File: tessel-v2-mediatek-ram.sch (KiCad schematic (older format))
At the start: 21 parts, among them U201 MT7620N, U301 W9751G6KB-25

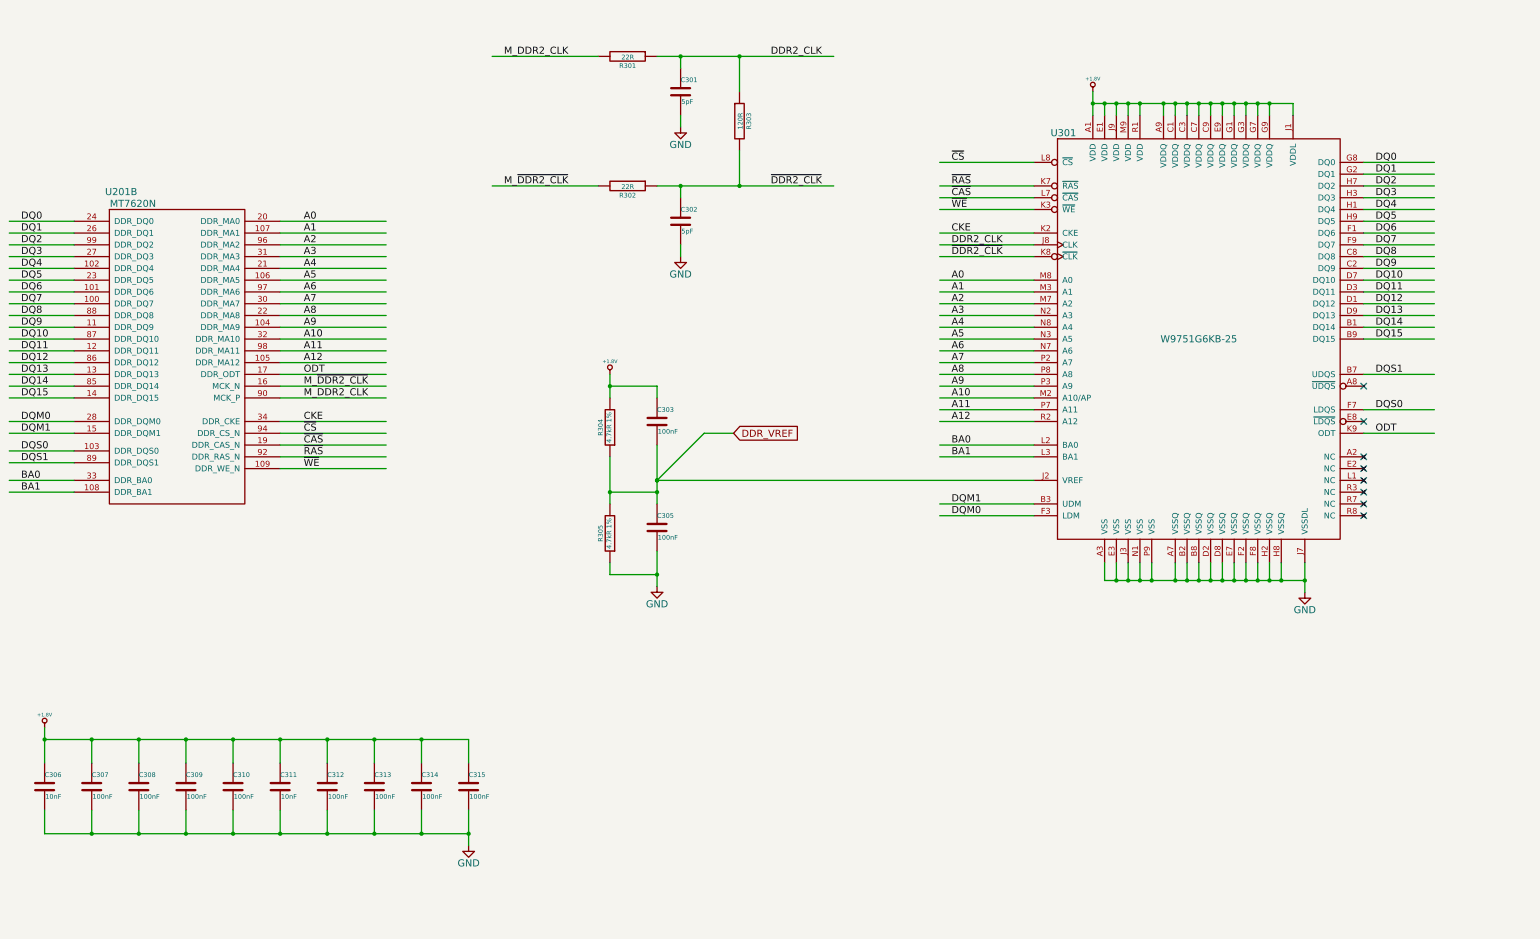
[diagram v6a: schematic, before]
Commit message: reset annotation
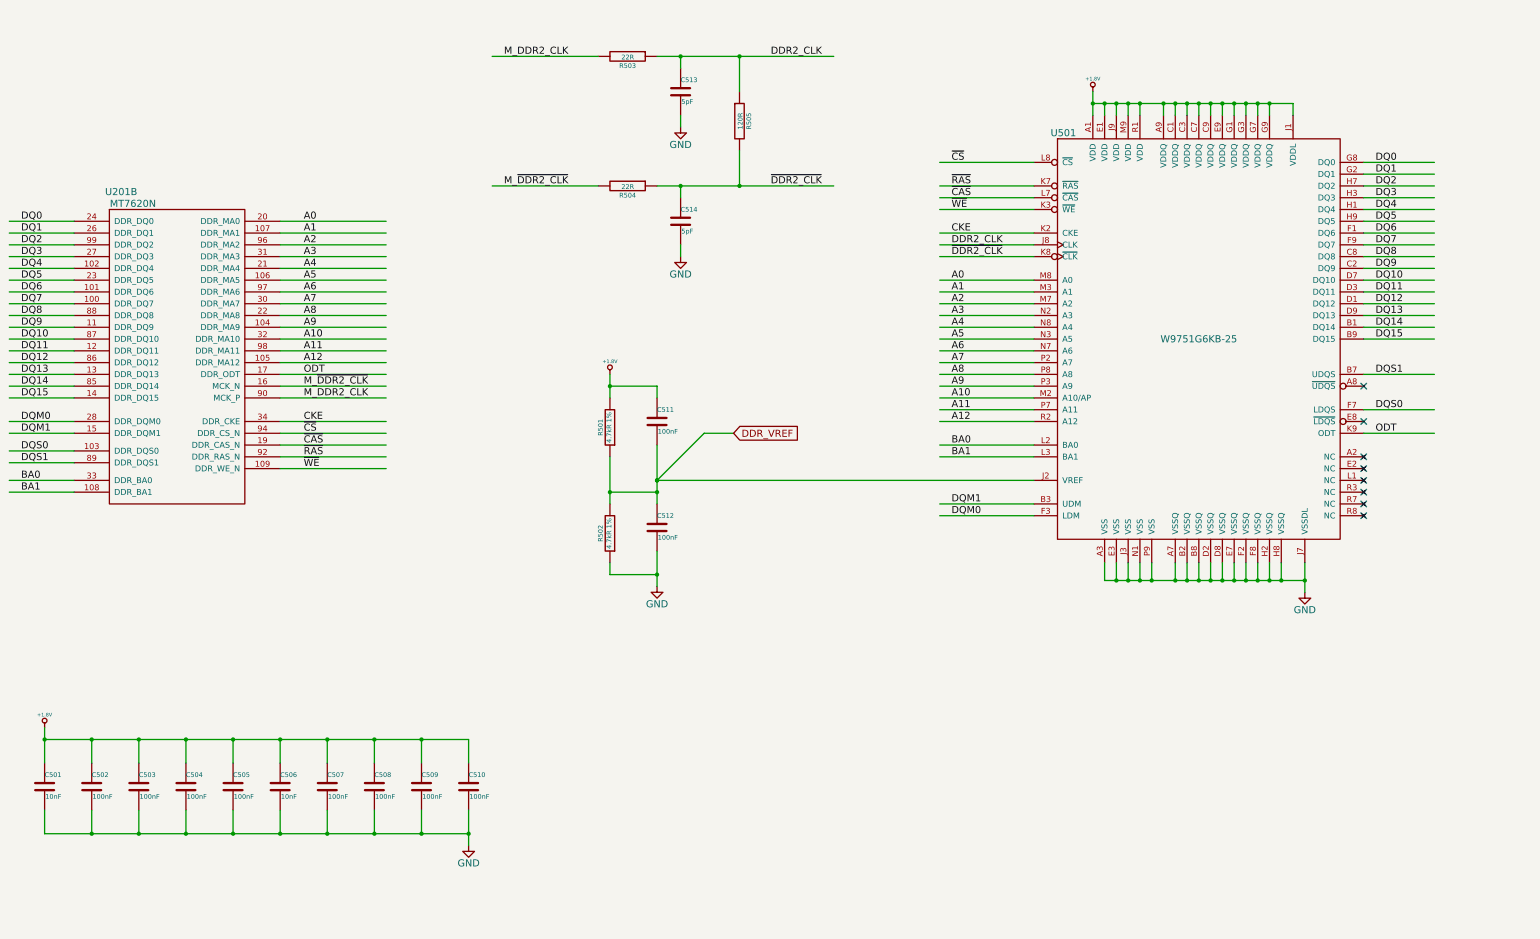
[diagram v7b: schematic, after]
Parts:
- renumbered C306 to C501, C307 to C502, C308 to C503, C309 to C504, C310 to C505, C311 to C506, C312 to C507, C313 to C508, C314 to C509, C315 to C510, C303 to C511, C305 to C512, C301 to C513, C302 to C514, R304 to R501, R305 to R502, R301 to R503, R302 to R504, R303 to R505, U301 to U501

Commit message: annotation did not take?
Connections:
- wire segments 222 -> 164
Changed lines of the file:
@@
 	11500 7000 11500 7150
 Wire Wire Line
-	11500 7150 11600 7150
-Wire Wire Line
-	11600 7150 11700 7150
-Wire Wire Line
-	11700 7150 11800 7150
-Wire Wire Line
-	11800 7150 11900 7150
-Wire Wire Line
-	11900 7150 12100 7150
-Wire Wire Line
-	12100 7150 12200 7150
-Wire Wire Line
-	12200 7150 12300 7150
-Wire Wire Line
-	12300 7150 12400 7150
-Wire Wire Line
-	12400 7150 12500 7150
-Wire Wire Line
-	12500 7150 12600 7150
-Wire Wire Line
-	12600 7150 12700 7150
-Wire Wire Line
-	12700 7150 12800 7150
-Wire Wire Line
-	12800 7150 12900 7150
-Wire Wire Line
-	12900 7150 13000 7150
-Wire Wire Line
-	13000 7150 13200 7150
+	11500 7150 13200 7150
 Wire Wire Line
 	11600 7150 11600 7000
@@
 Connection ~ 12200 7150
 Wire Wire Line
-	13200 7000 13200 7150
-Wire Wire Line
-	13200 7150 13200 7250
+	13200 7000 13200 7250
 Wire Wire Line
 	12400 7150 12400 7000
@@
 	4500 5600 5400 5600
 Wire Wire Line
-	7700 2700 7900 2700
-Wire Wire Line
-	7900 2700 8400 2700
-Wire Wire Line
-	8400 2700 9200 2700
+	7700 2700 9200 2700
 Wire Wire Line
 	7900 2800 7900 2700
@@
 	6300 3800 7200 3800
 Wire Wire Line
-	11400 3100 11500 3100
-Wire Wire Line
-	11500 3100 11600 3100
-Wire Wire Line
-	11600 3100 11700 3100
-Wire Wire Line
-	11700 3100 11800 3100
-Wire Wire Line
-	11800 3100 12000 3100
-Wire Wire Line
-	12000 3100 12100 3100
-Wire Wire Line
-	12100 3100 12200 3100
-Wire Wire Line
-	12200 3100 12300 3100
-Wire Wire Line
-	12300 3100 12400 3100
-Wire Wire Line
-	12400 3100 12500 3100
-Wire Wire Line
-	12500 3100 12600 3100
-Wire Wire Line
-	12600 3100 12700 3100
-Wire Wire Line
-	12700 3100 12800 3100
-Wire Wire Line
-	12800 3100 12900 3100
-Wire Wire Line
-	12900 3100 13100 3100
-Wire Wire Line
-	11400 3000 11400 3100
-Wire Wire Line
-	11400 3100 11400 3200
+	11400 3100 13100 3100
+Wire Wire Line
+	11400 3000 11400 3200
 Wire Wire Line
 	11500 3200 11500 3100
@@
 Connection ~ 12900 3100
 Wire Wire Line
-	2500 8400 2500 8500
-Wire Wire Line
-	2500 8500 2500 8700
-Wire Wire Line
-	2500 8500 2900 8500
-Wire Wire Line
-	2900 8500 3300 8500
-Wire Wire Line
-	3300 8500 3700 8500
-Wire Wire Line
-	3700 8500 4100 8500
-Wire Wire Line
-	4100 8500 4500 8500
-Wire Wire Line
-	4500 8500 4900 8500
-Wire Wire Line
-	4900 8500 5300 8500
-Wire Wire Line
-	5300 8500 5700 8500
-Wire Wire Line
-	5700 8500 6100 8500
+	2500 8400 2500 8700
+Wire Wire Line
+	2500 8500 6100 8500
 Wire Wire Line
 	2900 8500 2900 8700
@@
 	4100 9300 4100 9100
 Wire Wire Line
-	2500 9300 2900 9300
-Wire Wire Line
-	2900 9300 3300 9300
-Wire Wire Line
-	3300 9300 3700 9300
-Wire Wire Line
-	3700 9300 4100 9300
-Wire Wire Line
-	4100 9300 4500 9300
-Wire Wire Line
-	4500 9300 4900 9300
-Wire Wire Line
-	4900 9300 5300 9300
-Wire Wire Line
-	5300 9300 5700 9300
-Wire Wire Line
-	5700 9300 6100 9300
+	2500 9300 6100 9300
 Wire Wire Line
 	3700 9300 3700 9100
@@
 Connection ~ 5700 8500
 Wire Wire Line
-	6100 9100 6100 9300
-Wire Wire Line
-	6100 9300 6100 9400
+	6100 9100 6100 9400
 Wire Wire Line
 	5700 9300 5700 9100
@@
 Connection ~ 4900 9300
 Wire Wire Line
-	7300 5400 7300 5500
-Wire Wire Line
-	7300 5500 7300 5600
+	7300 5400 7300 5600
 Wire Wire Line
 	7700 5500 7700 5600
 Wire Wire Line
-	7700 6000 7700 6300
-Wire Wire Line
-	7700 6300 7700 6400
-Wire Wire Line
-	7700 6400 7700 6500
-Wire Wire Line
-	7300 6100 7300 6400
-Wire Wire Line
-	7300 6400 7300 6500
+	7700 6000 7700 6500
+Wire Wire Line
+	7300 6100 7300 6500
 Wire Wire Line
 	7300 6400 7700 6400
@@
 Connection ~ 13200 7150
 Wire Wire Line
-	7700 6900 7700 7100
-Wire Wire Line
-	7700 7100 7700 7200
+	7700 6900 7700 7200
 Wire Wire Line
 	7300 7100 7700 7100
@@
 	10900 4400 10100 4400
 Wire Wire Line
-	7700 3800 7900 3800
-Wire Wire Line
-	7900 3800 8400 3800
-Wire Wire Line
-	8400 3800 9200 3800
+	7700 3800 9200 3800
 Wire Wire Line
 	7900 3800 7900 3900
@@
 Connection ~ 4100 8500
 Wire Wire Line
-	10900 6300 7700 6300
-Wire Wire Line
-	7700 6300 7700 6300
+	7700 6300 10900 6300
 Wire Wire Line
 	8350 5900 8100 5900
 Wire Wire Line
 	8100 5900 7700 6300
-Connection ~ 7700 6300
 $Comp
 L MT7620N U?
